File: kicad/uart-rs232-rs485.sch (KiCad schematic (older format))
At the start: 21 parts, among them U10 MAX3232, U11 YD3082EESA

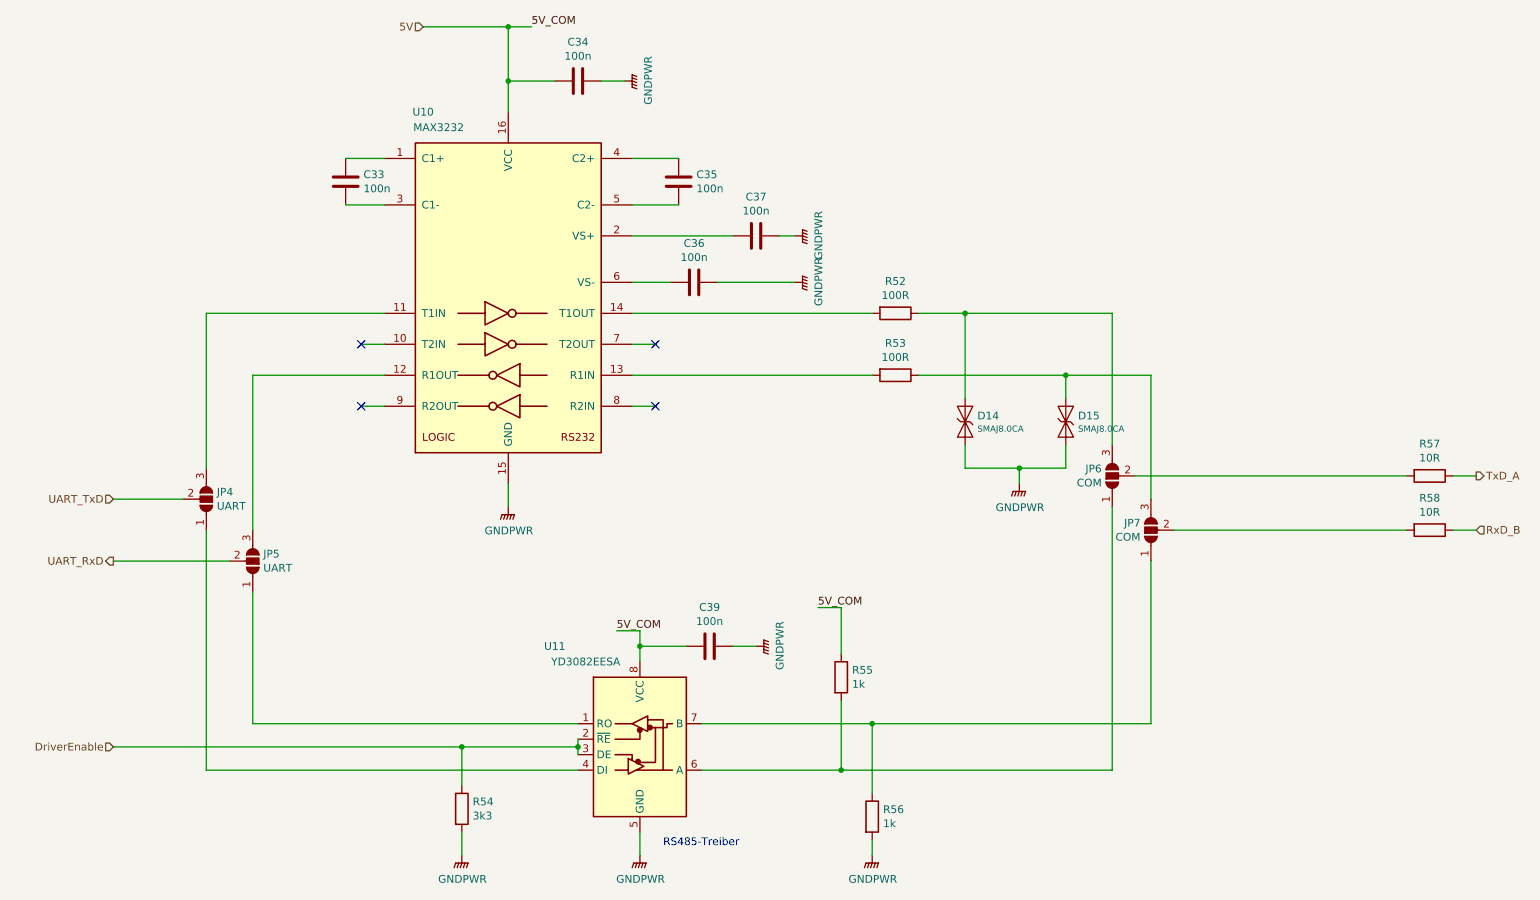
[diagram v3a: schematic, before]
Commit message: Layout Fertig, TODOs: Beschriftungen fertig stellen, ...
RS485 TVS-Diode
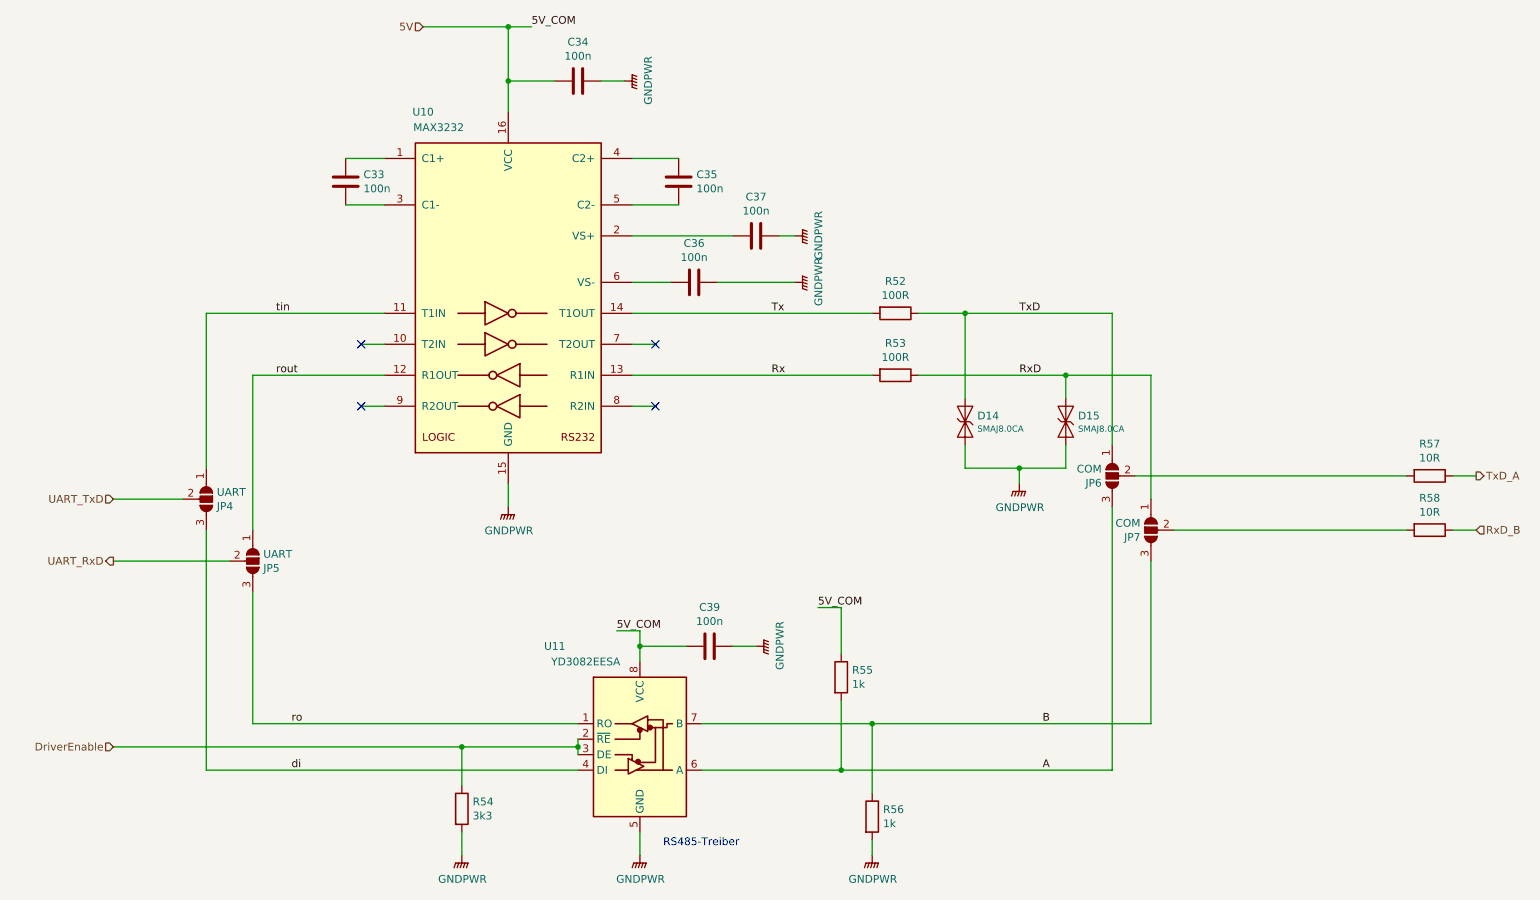
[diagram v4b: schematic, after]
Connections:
- net di: now reaches JP4.3 (B)
- net di: now also U11.4 (DI); no longer U10.11 (T1IN)
- net ro: now reaches JP5.3 (B)
- net ro: now also U11.1 (RO); no longer U10.12 (R1OUT)
- net Rx: now reaches R53.2, U10.13 (R1IN)
- net Tx: now reaches R52.2, U10.14 (T1OUT)
- net rout: now reaches JP5.1 (A)
- net rout: now also U10.12 (R1OUT); no longer U11.1 (RO)
- net tin: now reaches JP4.1 (A)
- net tin: now also U10.11 (T1IN); no longer U11.4 (DI)
- net A: now reaches R55.2, U11.6 (A)
- net A: now also JP6.3 (B); no longer JP6.1 (A)
- net B: now reaches R56.1, U11.7 (B)
- net B: now also JP7.3 (B); no longer JP7.1 (A)
- net TxD: now reaches D14.1 (A), R52.1
- net TxD: now also JP6.1 (A); no longer JP6.3 (B)
- net RxD: now reaches D15.1 (A), R53.1
- net RxD: now also JP7.1 (A); no longer JP7.3 (B)
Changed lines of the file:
@@
 F 3 "~" H 8100 3800 50  0001 C CNN
 	1    8100 3800
-	0    -1   -1   0
+	0    -1   1    0
 $EndComp
 $Comp
@@
 F 3 "~" H 8350 4150 50  0001 C CNN
 	1    8350 4150
-	0    -1   -1   0
+	0    -1   1    0
 $EndComp
 Wire Wire Line
@@
 F 3 "~" H 2250 3950 50  0001 C CNN
 	1    2250 3950
-	0    1    -1   0
+	0    1    1    0
 $EndComp
 $Comp
@@
 F 3 "~" H 2550 4350 50  0001 C CNN
 	1    2550 4350
-	0    1    -1   0
+	0    1    1    0
 $EndComp
 Wire Wire Line
@@
 	0    -1   -1   0
 $EndComp
+Text Label 7650 5400 0    50   ~ 0
+B
+Text Label 7650 5700 0    50   ~ 0
+A
+Text Label 7500 2750 0    50   ~ 0
+TxD
+Text Label 7500 3150 0    50   ~ 0
+RxD
+Text Label 5900 3150 0    50   ~ 0
+Rx
+Text Label 5900 2750 0    50   ~ 0
+Tx
+Text Label 2700 2750 0    50   ~ 0
+tin
+Text Label 2700 3150 0    50   ~ 0
+rout
+Text Label 2800 5400 0    50   ~ 0
+ro
+Text Label 2800 5700 0    50   ~ 0
+di
 $EndSCHEMATC

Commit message: Neu: Spannungsreferenz TL431, Laout Fertig, TODO: Labels
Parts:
- U11: footprint Package_SO:SO-8_3.9x4.9mm_P1.27mm -> Package_SO:SOIC-8_3.9x4.9mm_P1.27mm
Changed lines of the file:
@@
 F 0 "U11" H 4500 6100 50  0000 C CNN
 F 1 "YD3082EESA" H 4700 6000 50  0000 C CNN
-F 2 "Package_SO:SO-8_3.9x4.9mm_P1.27mm" H 5050 4800 50  0001 C CNN
+F 2 "Package_SO:SOIC-8_3.9x4.9mm_P1.27mm" H 5050 4800 50  0001 C CNN
 F 3 "https://datasheet.lcsc.com/lcsc/2006151006_GATEMODE-YD3082EESA_C269866.pdf" H 5050 5550 50  0001 C CNN
 F 4 "C269866" H 5050 5500 50  0001 C CNN "DistOrderNr"

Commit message: wip, bugfixes für v21.0.1
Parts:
- R52, R53: DistOrderNr C113307 -> C245445; ManPartNr RC1206JR-07100RL -> CR1206F100RP05Z; Manufacturer YAGEO -> Ever Ohms Tech; Notes 100Ω ±5% 0.25W ±100ppm/℃ 1206 Chip Resistor -> 0.25W ±1% ±100ppm/℃ 100Ω 1206; PriceEUR 0.0037 -> 0.0030
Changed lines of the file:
@@
 Sheet 9 10
 Title "HTL Lötregler Mini"
-Date "2021-06-01"
-Rev "21.0.0"
+Date "2021-09-22"
+Rev "21.0.1-dev"
 Comp "HTL Steyr"
 Comment1 "Prof. Karl Zeilhofer et al."
@@
 F 2 "Resistor_SMD:R_1206_3216Metric" V 6630 2750 50  0001 C CNN
 F 3 "~" H 6700 2750 50  0001 C CNN
-F 4 "0.0037" H 6700 2750 50  0001 C CNN "PriceEUR"
-F 5 "C113307" H 6700 2750 50  0001 C CNN "DistOrderNr"
+F 4 "0.0030" H 6700 2750 50  0001 C CNN "PriceEUR"
+F 5 "C245445" H 6700 2750 50  0001 C CNN "DistOrderNr"
 F 6 "LCSC" H 6700 2750 50  0001 C CNN "Distributor"
-F 7 "RC1206JR-07100RL" H 6700 2750 50  0001 C CNN "ManPartNr"
-F 8 "YAGEO" H 6700 2750 50  0001 C CNN "Manufacturer"
-F 9 "100Ω ±5% 0.25W ±100ppm/℃ 1206 Chip Resistor" H 6700 2750 50  0001 C CNN "Notes"
+F 7 "CR1206F100RP05Z" H 6700 2750 50  0001 C CNN "ManPartNr"
+F 8 "Ever Ohms Tech" H 6700 2750 50  0001 C CNN "Manufacturer"
+F 9 "0.25W ±1% ±100ppm/℃ 100Ω 1206" H 6700 2750 50  0001 C CNN "Notes"
 F 10 "500" H 6700 2750 50  0001 C CNN "PriceForQty"
 	1    6700 2750
@@
 F 2 "Resistor_SMD:R_1206_3216Metric" V 6630 3150 50  0001 C CNN
 F 3 "~" H 6700 3150 50  0001 C CNN
-F 4 "0.0037" H 6700 3150 50  0001 C CNN "PriceEUR"
-F 5 "C113307" H 6700 3150 50  0001 C CNN "DistOrderNr"
+F 4 "0.0030" H 6700 3150 50  0001 C CNN "PriceEUR"
+F 5 "C245445" H 6700 3150 50  0001 C CNN "DistOrderNr"
 F 6 "LCSC" H 6700 3150 50  0001 C CNN "Distributor"
-F 7 "RC1206JR-07100RL" H 6700 3150 50  0001 C CNN "ManPartNr"
-F 8 "YAGEO" H 6700 3150 50  0001 C CNN "Manufacturer"
-F 9 "100Ω ±5% 0.25W ±100ppm/℃ 1206 Chip Resistor" H 6700 3150 50  0001 C CNN "Notes"
+F 7 "CR1206F100RP05Z" H 6700 3150 50  0001 C CNN "ManPartNr"
+F 8 "Ever Ohms Tech" H 6700 3150 50  0001 C CNN "Manufacturer"
+F 9 "0.25W ±1% ±100ppm/℃ 100Ω 1206" H 6700 3150 50  0001 C CNN "Notes"
 F 10 "500" H 6700 3150 50  0001 C CNN "PriceForQty"
 	1    6700 3150

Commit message: BOM aktualisiert, Zenerdiode: Pinout IPC-konform gestaltet, ...
siehe https://gitlab.com/kicad/libraries/kicad-symbols/-/issues/3157
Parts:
- C33, C34, C35, C36, C37, C39: Index (none) -> 40
- D14, D15: Index (none) -> 45
- JP4, JP5, JP6, JP7: DistOrderNr (none) -> NAP4; Distributor (none) -> NAP; Index (none) -> 54
- R52, R53: Index (none) -> 28
- R54: Index (none) -> 26
- R55, R56: Index (none) -> 12
- R57, R58: DistOrderNr (none) -> R3216-10R; Distributor (none) -> AufLager; Index (none) -> 56
- U10: Index (none) -> 39
- U11: Distributor (none) -> LCSC; Index (none) -> 30; ManPartNr (none) -> YD3082EESA; Manufacturer (none) -> GATEMODE; Notes (none) -> 1Mbps RS422, RS485 Transceiver SOP-8 RS-485/RS-422; PriceEUR (none) -> 0.237; PriceForQty (none) -> 30; Weblink (none) -> https://lcsc.com/search?q=YD3082EESA
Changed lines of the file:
@@
 F 10 "https://lcsc.com/product-detail/Uncategorized_HGSEMI-MAX3232EIM-TR_C434486.html" H 4200 2650 50  0001 C CNN "Weblink"
 F 11 "RS232 - UART Umsetzer, 3V3 oder 5V" H 4200 2650 50  0001 C CNN "Notes"
+F 12 "39" H 4200 2650 50  0001 C CNN "Index"
 	1    4200 2650
 	1    0    0    -1
@@
 F 12 "C464972" H 5300 1900 50  0001 C CNN "DistOrderNr"
 F 13 "FN31X104K500PXG" H 5300 1900 50  0001 C CNN "ManPartNr"
+F 14 "40" H 5300 1900 50  0001 C CNN "Index"
+F 15 "" H 5300 1900 50  0001 C CNN "NotesAlt"
 	1    5300 1900
 	1    0    0    -1
@@
 F 12 "C464972" H 3150 1900 50  0001 C CNN "DistOrderNr"
 F 13 "FN31X104K500PXG" H 3150 1900 50  0001 C CNN "ManPartNr"
+F 14 "40" H 3150 1900 50  0001 C CNN "Index"
+F 15 "" H 3150 1900 50  0001 C CNN "NotesAlt"
 	1    3150 1900
 	1    0    0    -1
@@
 F 12 "C464972" H 5800 2250 50  0001 C CNN "DistOrderNr"
 F 13 "FN31X104K500PXG" H 5800 2250 50  0001 C CNN "ManPartNr"
+F 14 "40" H 5800 2250 50  0001 C CNN "Index"
+F 15 "" H 5800 2250 50  0001 C CNN "NotesAlt"
 	1    5800 2250
 	0    1    1    0
@@
 F 12 "C464972" H 5400 2550 50  0001 C CNN "DistOrderNr"
 F 13 "FN31X104K500PXG" H 5400 2550 50  0001 C CNN "ManPartNr"
+F 14 "40" H 5400 2550 50  0001 C CNN "Index"
+F 15 "" H 5400 2550 50  0001 C CNN "NotesAlt"
 	1    5400 2550
 	0    1    1    0
@@
 F 10 "C464972" H 4650 1250 50  0001 C CNN "DistOrderNr"
 F 11 "FN31X104K500PXG" H 4650 1250 50  0001 C CNN "ManPartNr"
+F 12 "40" H 4650 1250 50  0001 C CNN "Index"
+F 13 "" H 4650 1250 50  0001 C CNN "NotesAlt"
 	1    4650 1250
 	0    1    1    0
@@
 F 9 "0.25W ±1% ±100ppm/℃ 100Ω 1206" H 6700 2750 50  0001 C CNN "Notes"
 F 10 "500" H 6700 2750 50  0001 C CNN "PriceForQty"
+F 11 "28" H 6700 2750 50  0001 C CNN "Index"
 	1    6700 2750
 	0    1    1    0
@@
 F 9 "0.25W ±1% ±100ppm/℃ 100Ω 1206" H 6700 3150 50  0001 C CNN "Notes"
 F 10 "500" H 6700 3150 50  0001 C CNN "PriceForQty"
+F 11 "28" H 6700 3150 50  0001 C CNN "Index"
 	1    6700 3150
 	0    1    1    0
@@
 F 10 "100" H 7150 3450 50  0001 C CNN "PriceForQty"
 F 11 "https://lcsc.com/product-detail/Pre-ordered-transistors_GOODWORK-SMAJ8-0CA_C908814.html" H 7150 3450 50  0001 C CNN "Weblink"
+F 12 "45" H 7150 3450 50  0001 C CNN "Index"
 	1    7150 3450
 	0    1    1    0
@@
 F 10 "100" H 7800 3450 50  0001 C CNN "PriceForQty"
 F 11 "https://lcsc.com/product-detail/Pre-ordered-transistors_GOODWORK-SMAJ8-0CA_C908814.html" H 7800 3450 50  0001 C CNN "Weblink"
+F 12 "45" H 7800 3450 50  0001 C CNN "Index"
 	1    7800 3450
 	0    1    1    0
@@
 F 3 "https://datasheet.lcsc.com/lcsc/2006151006_GATEMODE-YD3082EESA_C269866.pdf" H 5050 5550 50  0001 C CNN
 F 4 "C269866" H 5050 5500 50  0001 C CNN "DistOrderNr"
+F 5 "LCSC" H 5050 5500 50  0001 C CNN "Distributor"
+F 6 "30" H 5050 5500 50  0001 C CNN "Index"
+F 7 "GATEMODE" H 5050 5500 50  0001 C CNN "Manufacturer"
+F 8 "YD3082EESA" H 5050 5500 50  0001 C CNN "ManPartNr"
+F 9 "0.237" H 5050 5500 50  0001 C CNN "PriceEUR"
+F 10 "30" H 5050 5500 50  0001 C CNN "PriceForQty"
+F 11 "https://lcsc.com/search?q=YD3082EESA" H 5050 5500 50  0001 C CNN "Weblink"
+F 12 "1Mbps RS422, RS485 Transceiver SOP-8 RS-485/RS-422" H 5050 5500 50  0001 C CNN "Notes"
 	1    5050 5500
 	1    0    0    -1
@@
 F 2 "Jumper:SolderJumper-3_P2.0mm_Open_TrianglePad1.0x1.5mm_NumberLabels" H 8100 3800 50  0001 C CNN
 F 3 "~" H 8100 3800 50  0001 C CNN
+F 4 "NAP4" H 8100 3800 50  0001 C CNN "DistOrderNr"
+F 5 "NAP" H 8100 3800 50  0001 C CNN "Distributor"
+F 6 "54" H 8100 3800 50  0001 C CNN "Index"
 	1    8100 3800
 	0    -1   1    0
@@
 F 2 "Jumper:SolderJumper-3_P2.0mm_Open_TrianglePad1.0x1.5mm_NumberLabels" H 8350 4150 50  0001 C CNN
 F 3 "~" H 8350 4150 50  0001 C CNN
+F 4 "NAP4" H 8350 4150 50  0001 C CNN "DistOrderNr"
+F 5 "NAP" H 8350 4150 50  0001 C CNN "Distributor"
+F 6 "54" H 8350 4150 50  0001 C CNN "Index"
 	1    8350 4150
 	0    -1   1    0
@@
 F 10 "C464972" H 5500 4900 50  0001 C CNN "DistOrderNr"
 F 11 "FN31X104K500PXG" H 5500 4900 50  0001 C CNN "ManPartNr"
+F 12 "40" H 5500 4900 50  0001 C CNN "Index"
+F 13 "" H 5500 4900 50  0001 C CNN "NotesAlt"
 	1    5500 4900
 	0    1    1    0
@@
 F 2 "Jumper:SolderJumper-3_P2.0mm_Open_TrianglePad1.0x1.5mm_NumberLabels" H 2250 3950 50  0001 C CNN
 F 3 "~" H 2250 3950 50  0001 C CNN
+F 4 "NAP4" H 2250 3950 50  0001 C CNN "DistOrderNr"
+F 5 "NAP" H 2250 3950 50  0001 C CNN "Distributor"
+F 6 "54" H 2250 3950 50  0001 C CNN "Index"
 	1    2250 3950
 	0    1    1    0
@@
 F 2 "Jumper:SolderJumper-3_P2.0mm_Open_TrianglePad1.0x1.5mm_NumberLabels" H 2550 4350 50  0001 C CNN
 F 3 "~" H 2550 4350 50  0001 C CNN
+F 4 "NAP4" H 2550 4350 50  0001 C CNN "DistOrderNr"
+F 5 "NAP" H 2550 4350 50  0001 C CNN "Distributor"
+F 6 "54" H 2550 4350 50  0001 C CNN "Index"
 	1    2550 4350
 	0    1    1    0
@@
 F 5 "C229599" H 3900 5950 50  0001 C CNN "DistOrderNr"
 F 6 "LCSC" H 3900 5950 50  0001 C CNN "Distributor"
+F 7 "26" H 3900 5950 50  0001 C CNN "Index"
 	1    3900 5950
 	1    0    0    -1
@@
 F 2 "Resistor_SMD:R_1206_3216Metric" V 10080 3800 50  0001 C CNN
 F 3 "~" H 10150 3800 50  0001 C CNN
+F 4 "R3216-10R" H 10150 3800 50  0001 C CNN "DistOrderNr"
+F 5 "AufLager" H 10150 3800 50  0001 C CNN "Distributor"
+F 6 "56" H 10150 3800 50  0001 C CNN "Index"
 	1    10150 3800
 	0    1    1    0
@@
 F 2 "Resistor_SMD:R_1206_3216Metric" V 10080 4150 50  0001 C CNN
 F 3 "~" H 10150 4150 50  0001 C CNN
+F 4 "R3216-10R" H 10150 4150 50  0001 C CNN "DistOrderNr"
+F 5 "AufLager" H 10150 4150 50  0001 C CNN "Distributor"
+F 6 "56" H 10150 4150 50  0001 C CNN "Index"
 	1    10150 4150
 	0    1    1    0
@@
 F 9 "1kΩ ±5% 0.25W ±100ppm/℃ 1206 Chip Resistor" H 6350 5100 50  0001 C CNN "Notes"
 F 10 "50" H 6350 5100 50  0001 C CNN "PriceForQty"
+F 11 "12" H 6350 5100 50  0001 C CNN "Index"
 	1    6350 5100
 	1    0    0    -1
@@
 F 9 "1kΩ ±5% 0.25W ±100ppm/℃ 1206 Chip Resistor" H 6550 6000 50  0001 C CNN "Notes"
 F 10 "50" H 6550 6000 50  0001 C CNN "PriceForQty"
+F 11 "12" H 6550 6000 50  0001 C CNN "Index"
 	1    6550 6000
 	1    0    0    -1
